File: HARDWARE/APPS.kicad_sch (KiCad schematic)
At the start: 22 parts, among them SW1 SW_Push, U1 STM32L4P5RET6, Y1 Crystal_GND24

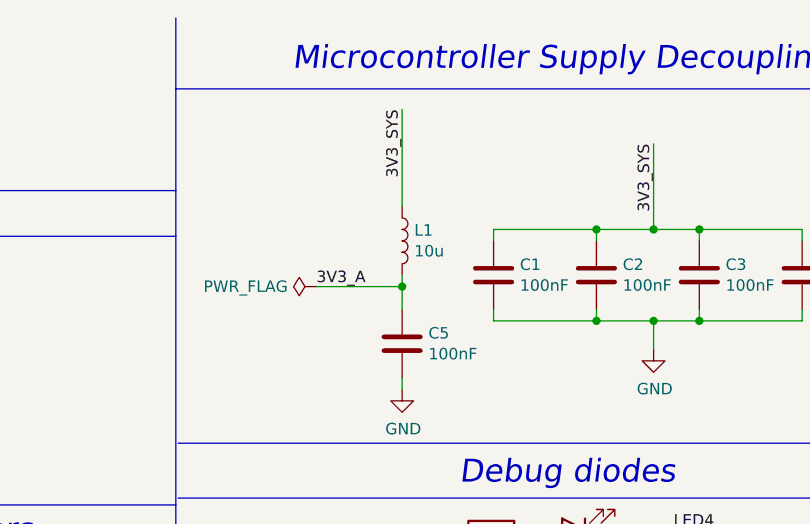
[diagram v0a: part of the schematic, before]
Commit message: Use in-amps for the analog inputs
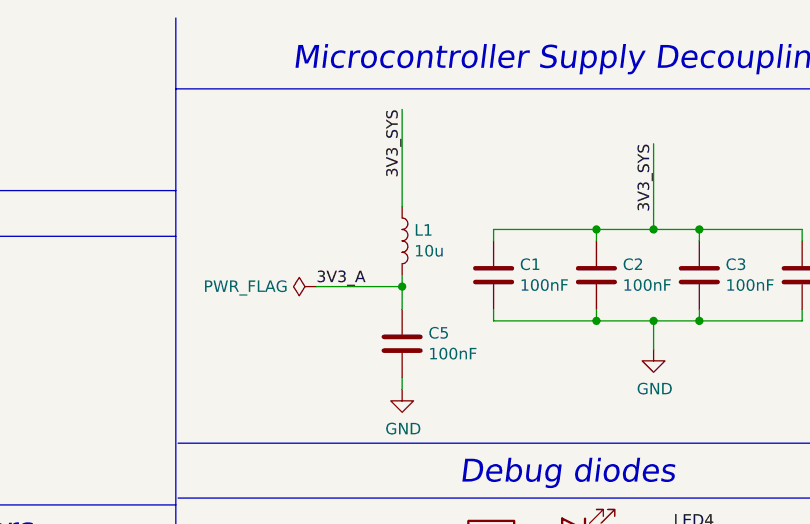
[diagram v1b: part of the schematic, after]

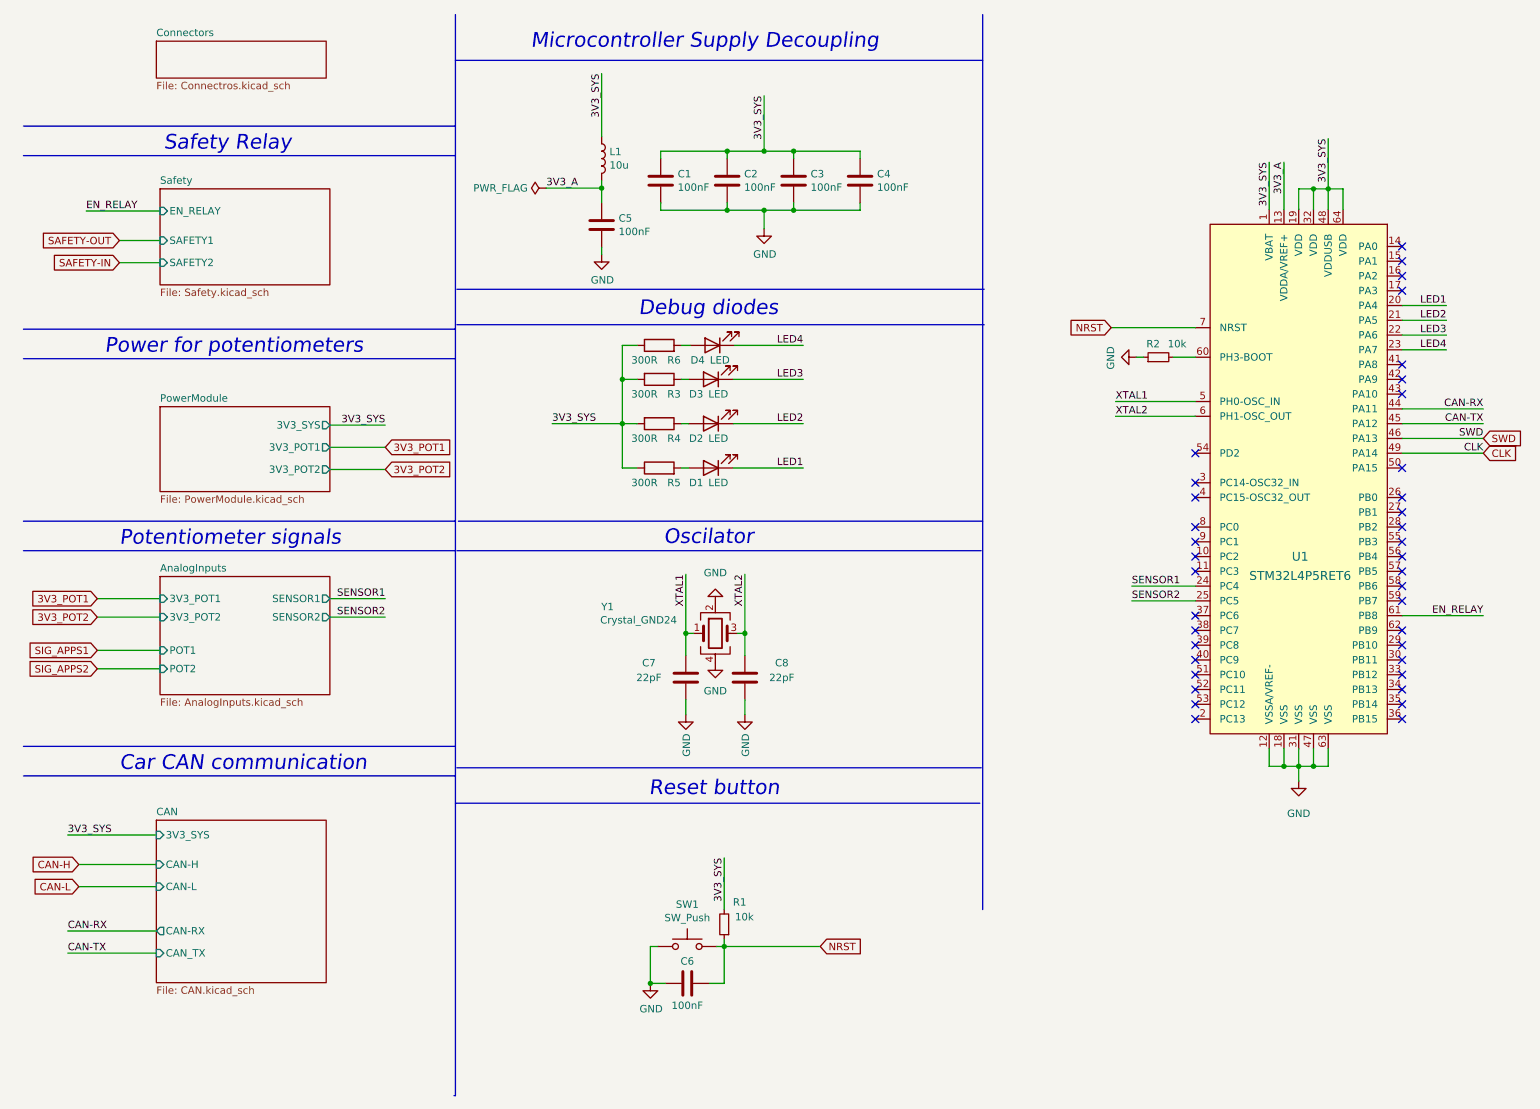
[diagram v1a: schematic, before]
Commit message: Align components on the PCB
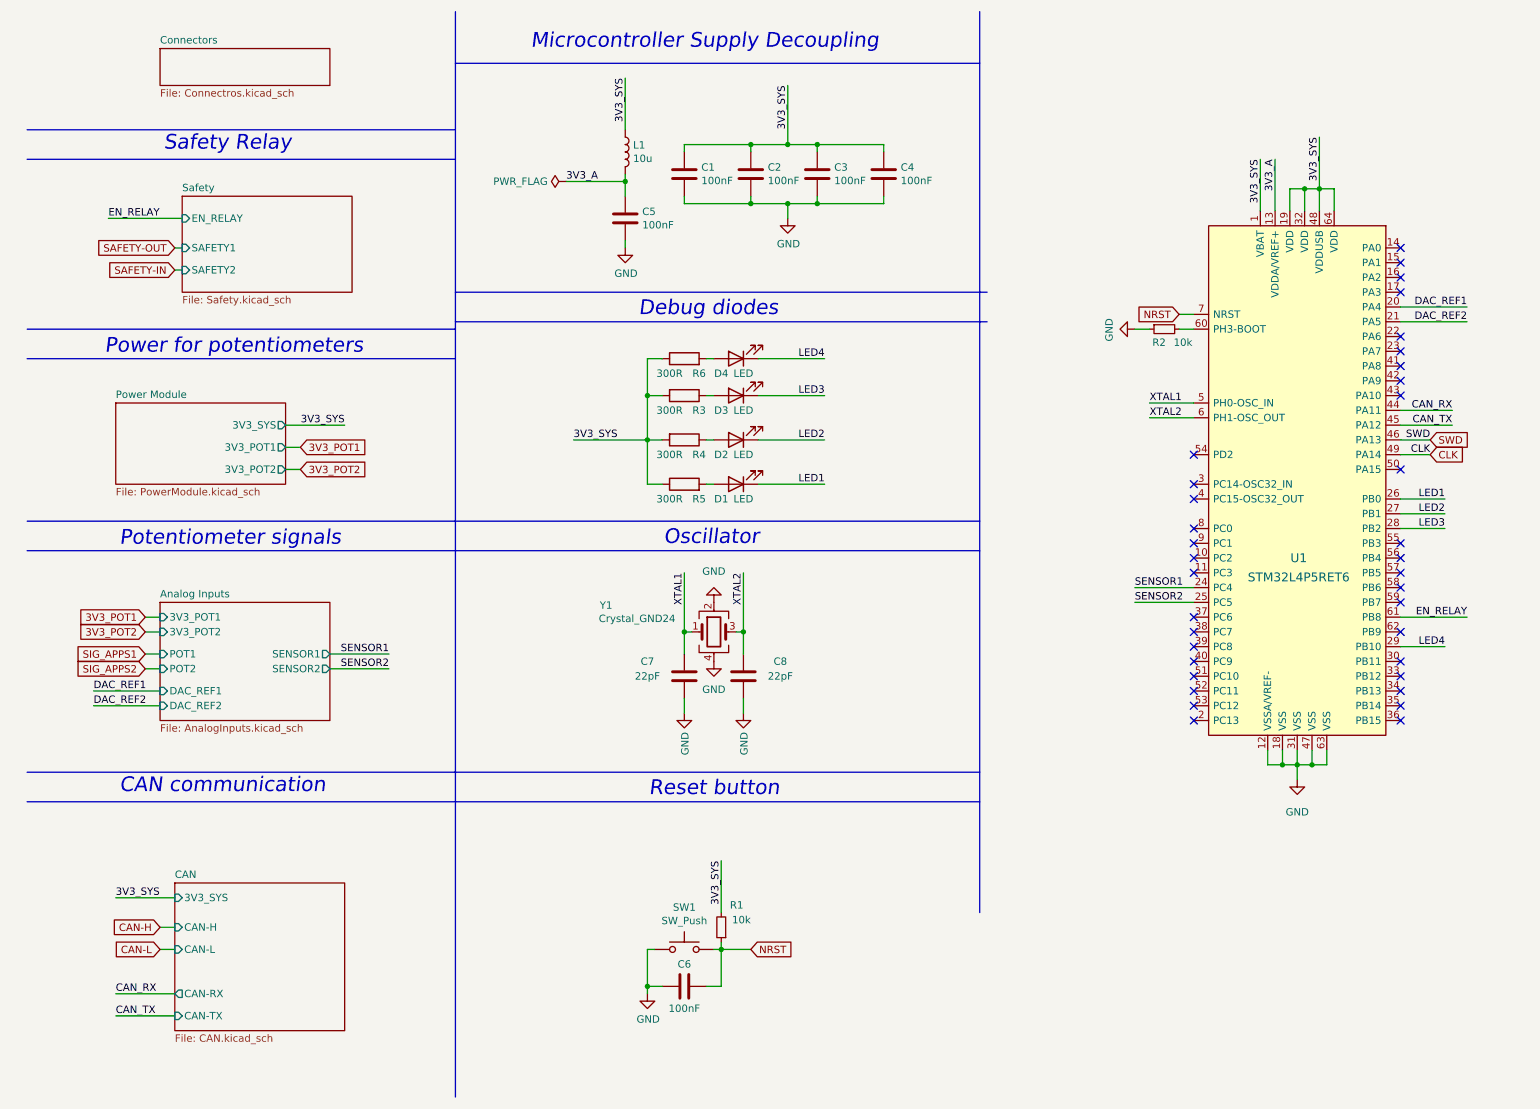
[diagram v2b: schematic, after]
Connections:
- net LED1: now also U1.26 (PB0); no longer U1.20 (PA4)
- net LED2: now also U1.27 (PB1); no longer U1.21 (PA5)
- net LED3: now also U1.28 (PB2); no longer U1.22 (PA6)
- net LED4: now also U1.29 (PB10); no longer U1.23 (PA7)
- net CAN-RX renamed CAN_RX
- net CAN-TX renamed CAN_TX
- new net DAC_REF1: U1.20 (PA4)
- new net DAC_REF2: U1.21 (PA5)
- no-connect marks 38 -> 36
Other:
- sheet AnalogInputs renamed Analog Inputs
- sheet PowerModule renamed Power Module
- sheet Analog Inputs ports: added DAC_REF1, DAC_REF2; removed none
- sheet CAN ports: added CAN-TX; removed CAN_TX
- note added: "CAN communication"
- note added: "Oscillator"
- note removed: "Car CAN communication"
- note removed: "Oscilator"
- company: (none) -> PUT Motorsport
- title: PUT Motorsport EV APPS -> APPS
- moved on the sheet: C1, C2, C3, C4, C5, C6, D1, D2, D3, D4, L1, R1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

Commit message: KiCad project refactor
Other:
- note added: "CAN Communication"
- note added: "Debug Diodes"
- note added: "MCU Power Supply Decoupling"
- note added: "Potentiometer Signals"
- note added: "Power for Potentiometers"
- note added: "Reset Button"
- note removed: "CAN communication"
- note removed: "Debug diodes"
- note removed: "Microcontroller Supply Decoupling"
- note removed: "Potentiometer signals"
- note removed: "Power for potentiometers"
- note removed: "Reset button"
- moved on the sheet: C6, R1, SW1
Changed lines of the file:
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@@
   (junction (at 232.41 41.91) (diameter 0) (color 0 0 0 0)
   )
-  (junction (at 132.08 172.72) (diameter 0) (color 0 0 0 0)
+  (junction (at 134.62 173.99) (diameter 0) (color 0 0 0 0)
   )
   (junction (at 148.59 34.29) (diameter 0) (color 0 0 0 0)
@@
   (junction (at 233.68 140.97) (diameter 0) (color 0 0 0 0)
   )
-  (junction (at 119.38 179.07) (diameter 0) (color 0 0 0 0)
+  (junction (at 121.92 180.34) (diameter 0) (color 0 0 0 0)
   )
   (junction (at 234.95 41.91) (diameter 0) (color 0 0 0 0)
@@
     (stroke (width 0) (type default))
   )
-  (polyline (pts (xy 86.36 20.32) (xy 176.53 20.32))
-    (stroke (width 0) (type default))
-  )
-  (wire (pts (xy 119.38 180.34) (xy 119.38 179.07))
+  (polyline (pts (xy 86.36 17.78) (xy 176.53 17.78))
+    (stroke (width 0) (type default))
+  )
+  (wire (pts (xy 121.92 181.61) (xy 121.92 180.34))
     (stroke (width 0) (type default))
   )
@@
     (stroke (width 0) (type default))
   )
-  (wire (pts (xy 119.38 172.72) (xy 120.65 172.72))
-    (stroke (width 0) (type default))
-  )
-  (wire (pts (xy 129.54 179.07) (xy 132.08 179.07))
+  (wire (pts (xy 121.92 173.99) (xy 123.19 173.99))
+    (stroke (width 0) (type default))
+  )
+  (wire (pts (xy 132.08 180.34) (xy 134.62 180.34))
     (stroke (width 0) (type default))
   )
@@
     (stroke (width 0) (type default))
   )
-  (wire (pts (xy 132.08 172.72) (xy 137.16 172.72))
+  (wire (pts (xy 134.62 173.99) (xy 139.7 173.99))
     (stroke (width 0) (type default))
   )
@@
     (stroke (width 0) (type default))
   )
-  (wire (pts (xy 132.08 157.48) (xy 132.08 166.37))
+  (wire (pts (xy 134.62 158.75) (xy 134.62 167.64))
     (stroke (width 0) (type default))
   )
@@
     (stroke (width 0) (type default))
   )
-  (wire (pts (xy 119.38 179.07) (xy 121.92 179.07))
+  (wire (pts (xy 121.92 180.34) (xy 124.46 180.34))
     (stroke (width 0) (type default))
   )
@@
     (stroke (width 0) (type default))
   )
-  (polyline (pts (xy 176.53 11.43) (xy 176.53 166.37))
-    (stroke (width 0) (type default))
-  )
-  (polyline (pts (xy 86.36 64.77) (xy 177.8 64.77))
+  (polyline (pts (xy 176.53 12.7) (xy 176.53 166.37))
+    (stroke (width 0) (type default))
+  )
+  (polyline (pts (xy 86.36 64.77) (xy 176.53 64.77))
     (stroke (width 0) (type default))
   )
@@
     (stroke (width 0) (type default))
   )
-  (wire (pts (xy 132.08 179.07) (xy 132.08 172.72))
+  (wire (pts (xy 134.62 180.34) (xy 134.62 173.99))
     (stroke (width 0) (type default))
   )
@@
     (stroke (width 0) (type default))
   )
-  (wire (pts (xy 119.38 179.07) (xy 119.38 172.72))
+  (wire (pts (xy 121.92 180.34) (xy 121.92 173.99))
     (stroke (width 0) (type default))
   )
@@
     (stroke (width 0) (type default))
   )
-  (polyline (pts (xy 86.36 11.43) (xy 86.36 198.12))
+  (polyline (pts (xy 86.36 12.7) (xy 86.36 198.12))
     (stroke (width 0) (type default))
   )
@@
     (stroke (width 0) (type default))
   )
-  (wire (pts (xy 132.08 171.45) (xy 132.08 172.72))
+  (wire (pts (xy 134.62 172.72) (xy 134.62 173.99))
     (stroke (width 0) (type default))
   )
@@
     (stroke (width 0) (type default))
   )
-  (wire (pts (xy 132.08 172.72) (xy 130.81 172.72))
+  (wire (pts (xy 134.62 173.99) (xy 133.35 173.99))
     (stroke (width 0) (type default))
   )
@@
     (stroke (width 0) (type default))
   )
-  (polyline (pts (xy 86.36 59.69) (xy 177.8 59.69))
-    (stroke (width 0) (type default))
-  )
-  (text "Power for potentiometers" (at 26.035 70.485 0)
+  (polyline (pts (xy 86.36 59.69) (xy 176.53 59.69))
+    (stroke (width 0) (type default))
+  )
+  (text "Power for Potentiometers" (at 24.765 70.485 0)
     (effects (font (size 2.54 2.54) italic) (justify left bottom))
   )
@@
     (effects (font (size 2.54 2.54) italic) (justify left bottom))
   )
-  (text "Reset button" (at 119.634 146.558 0)
+  (text "Reset Button" (at 119.634 146.558 0)
     (effects (font (size 2.54 2.54) italic) (justify left bottom))
   )
@@
     (effects (font (size 2.54 2.54) italic) (justify left bottom))
   )
-  (text "Microcontroller Supply Decoupling" (at 99.314 18.034 0)
+  (text "MCU Power Supply Decoupling" (at 103.124 16.764 0)
     (effects (font (size 2.54 2.54) italic) (justify left bottom))
   )
-  (text "Debug diodes\n" (at 117.856 64.008 0)
+  (text "Debug Diodes\n" (at 117.856 64.008 0)
     (effects (font (size 2.54 2.54) italic) (justify left bottom))
   )
-  (text "Potentiometer signals" (at 28.575 103.505 0)
+  (text "Potentiometer Signals" (at 28.575 103.505 0)
     (effects (font (size 2.54 2.54) italic) (justify left bottom))
   )
-  (text "CAN communication" (at 28.575 146.05 0)
+  (text "CAN Communication" (at 28.575 146.05 0)
     (effects (font (size 2.54 2.54) italic) (justify left bottom))
   )
@@
     (effects (font (size 1.27 1.27)) (justify right bottom))
   )
-  (label "3V3_SYS" (at 132.08 157.48 270) (fields_autoplaced)
+  (label "3V3_SYS" (at 134.62 158.75 270) (fields_autoplaced)
     (effects (font (size 1.27 1.27)) (justify right bottom))
   )
@@
     )
   )
-  (global_label "NRST" (shape input) (at 137.16 172.72 0) (fields_autoplaced)
+  (global_label "NRST" (shape input) (at 139.7 173.99 0) (fields_autoplaced)
     (effects (font (size 1.27 1.27)) (justify left))
-    (property "Intersheetrefs" "${INTERSHEET_REFS}" (at 144.2618 172.7994 0)
+    (property "Intersheetrefs" "${INTERSHEET_REFS}" (at 146.8018 174.0694 0)
       (effects (font (size 1.27 1.27)) (justify left) hide)
     )
@@
     )
   )
-  (symbol (lib_id "Device:C") (at 125.73 179.07 270) (unit 1)
-    (in_bom yes) (on_board yes) (dnp no)
-    (property "Reference" "C6" (at 125.73 175.26 90)
-      (effects (font (size 1.27 1.27)))
-    )
-    (property "Value" "100nF" (at 125.73 182.88 90)
-      (effects (font (size 1.27 1.27)))
-    )
-    (property "Footprint" "Capacitor_SMD:C_0603_1608Metric_Pad1.08x0.95mm_HandSolder" (at 121.92 180.0352 0)
-      (effects (font (size 1.27 1.27)) hide)
-    )
-    (property "Datasheet" "~" (at 125.73 179.07 0)
+  (symbol (lib_id "Device:C") (at 128.27 180.34 270) (unit 1)
+    (in_bom yes) (on_board yes) (dnp no)
+    (property "Reference" "C6" (at 128.27 176.53 90)
+      (effects (font (size 1.27 1.27)))
+    )
+    (property "Value" "100nF" (at 128.27 184.15 90)
+      (effects (font (size 1.27 1.27)))
+    )
+    (property "Footprint" "Capacitor_SMD:C_0603_1608Metric_Pad1.08x0.95mm_HandSolder" (at 124.46 181.3052 0)
+      (effects (font (size 1.27 1.27)) hide)
+    )
+    (property "Datasheet" "~" (at 128.27 180.34 0)
       (effects (font (size 1.27 1.27)) hide)
     )
@@
     )
   )
-  (symbol (lib_id "Switch:SW_Push") (at 125.73 172.72 0) (unit 1)
-    (in_bom yes) (on_board yes) (dnp no)
-    (property "Reference" "SW1" (at 125.73 165.481 0)
-      (effects (font (size 1.27 1.27)))
-    )
-    (property "Value" "SW_Push" (at 125.73 167.7924 0)
-      (effects (font (size 1.27 1.27)))
-    )
-    (property "Footprint" "Button_Switch_THT:SW_PUSH_6mm" (at 125.73 167.64 0)
-      (effects (font (size 1.27 1.27)) hide)
-    )
-    (property "Datasheet" "" (at 125.73 167.64 0)
+  (symbol (lib_id "Switch:SW_Push") (at 128.27 173.99 0) (unit 1)
+    (in_bom yes) (on_board yes) (dnp no)
+    (property "Reference" "SW1" (at 128.27 166.751 0)
+      (effects (font (size 1.27 1.27)))
+    )
+    (property "Value" "SW_Push" (at 128.27 169.0624 0)
+      (effects (font (size 1.27 1.27)))
+    )
+    (property "Footprint" "Button_Switch_THT:SW_PUSH_6mm" (at 128.27 168.91 0)
+      (effects (font (size 1.27 1.27)) hide)
+    )
+    (property "Datasheet" "" (at 128.27 168.91 0)
       (effects (font (size 1.27 1.27)) hide)
     )
@@
     )
   )
-  (symbol (lib_id "power:GND") (at 119.38 180.34 0) (unit 1)
-    (in_bom yes) (on_board yes) (dnp no)
-    (property "Reference" "#PWR03" (at 119.38 186.69 0)
-      (effects (font (size 1.27 1.27)) hide)
-    )
-    (property "Value" "GND" (at 119.507 184.7342 0)
-      (effects (font (size 1.27 1.27)))
-    )
-    (property "Footprint" "" (at 119.38 180.34 0)
-      (effects (font (size 1.27 1.27)) hide)
-    )
-    (property "Datasheet" "" (at 119.38 180.34 0)
+  (symbol (lib_id "power:GND") (at 121.92 181.61 0) (unit 1)
+    (in_bom yes) (on_board yes) (dnp no)
+    (property "Reference" "#PWR03" (at 121.92 187.96 0)
+      (effects (font (size 1.27 1.27)) hide)
+    )
+    (property "Value" "GND" (at 122.047 186.0042 0)
+      (effects (font (size 1.27 1.27)))
+    )
+    (property "Footprint" "" (at 121.92 181.61 0)
+      (effects (font (size 1.27 1.27)) hide)
+    )
+    (property "Datasheet" "" (at 121.92 181.61 0)
       (effects (font (size 1.27 1.27)) hide)
     )
@@
     )
   )
-  (symbol (lib_id "Device:R_Small") (at 132.08 168.91 180) (unit 1)
-    (in_bom yes) (on_board yes) (dnp no)
-    (property "Reference" "R1" (at 135.89 165.1 0)
-      (effects (font (size 1.27 1.27)) (justify left))
-    )
-    (property "Value" "10k" (at 137.16 167.64 0)
-      (effects (font (size 1.27 1.27)) (justify left))
-    )
-    (property "Footprint" "Resistor_SMD:R_0603_1608Metric_Pad0.98x0.95mm_HandSolder" (at 132.08 168.91 0)
-      (effects (font (size 1.27 1.27)) hide)
-    )
-    (property "Datasheet" "~" (at 132.08 168.91 0)
-      (effects (font (size 1.27 1.27)) hide)
-    )
+  (symbol (lib_id "Device:R_Small") (at 134.62 170.18 180) (unit 1)
+    (in_bom yes) (on_board yes) (dnp no)
+    (property "Reference" "R1" (at 138.43 166.37 0)
+      (effects (font (size 1.27 1.27)) (justify left))
+    )
+    (property "Value" "10k" (at 139.7 168.91 0)
+      (effects (font (size 1.27 1.27)) (justify left))
+    )
+    (property "Footprint" "Resistor_SMD:R_0603_1608Metric_Pad0.98x0.95mm_HandSolder" (at 134.62 170.18 0)
+      (effects (font (size 1.27 1.27)) hide)
+    )
+    (property "Datasheet" "~" (at 134.62 170.18 0)
+      (effects (font (size 1.27 1.27)) hide)
+    )

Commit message: Route PCB tracks
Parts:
- C1: renamed from C5; value 100nF -> 100n
- C2: renamed from C1; value 100nF -> 100n
- C3: renamed from C7; value 22pF -> 22p
- C4: renamed from C6; value 100nF -> 100n
- C5: renamed from C8; value 22pF -> 22p
- C6: renamed from C2; value 100nF -> 100n
- C7: renamed from C3; value 100nF -> 100n
- C8: renamed from C4; value 100nF -> 100n
- Y1: value Crystal_GND24 -> 8Mhz; footprint Crystal:Crystal_SMD_2520-4Pin_2.5x2.0mm -> Crystal:Crystal_SMD_3225-4Pin_3.2x2.5mm
- renumbered D4 to D1, D3 to D2, D2 to D3, D1 to D4, R6 to R1, R3 to R2, R4 to R3, R5 to R4, R1 to R5, R2 to R6
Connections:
- net XTAL1: now also Y1.3; no longer Y1.1
- net XTAL2: now also Y1.1; no longer Y1.3
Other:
- company: PUT Motorsport -> S. Sambor
- title: APPS -> Accelerator Pedal Position Sensor
